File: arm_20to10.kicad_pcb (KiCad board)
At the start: 2 copper layers, 16.9 x 29.7 mm, 10 parts, among them J1 SFH11-PBPC-D10-RA-BK, J2 20021111-00010T4LF, SW1 SSSS810701, U1 MIC5504-3.3YM5 TR

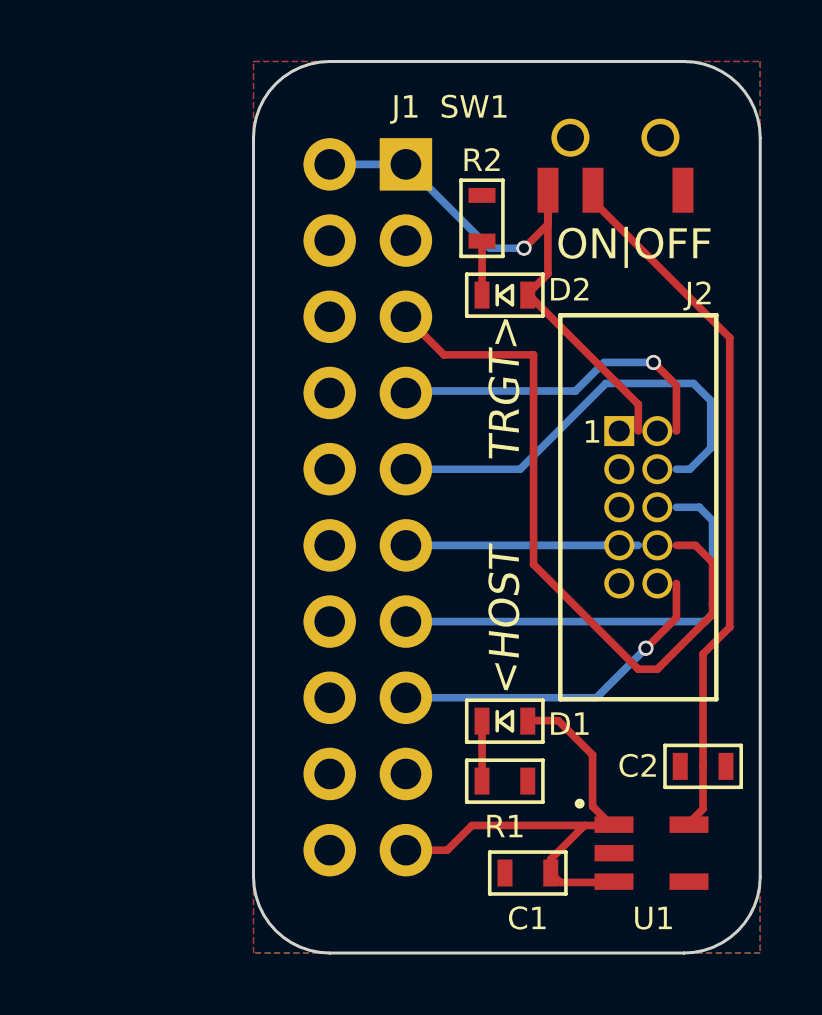
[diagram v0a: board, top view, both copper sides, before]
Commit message: Moved to the Kicad 9.0
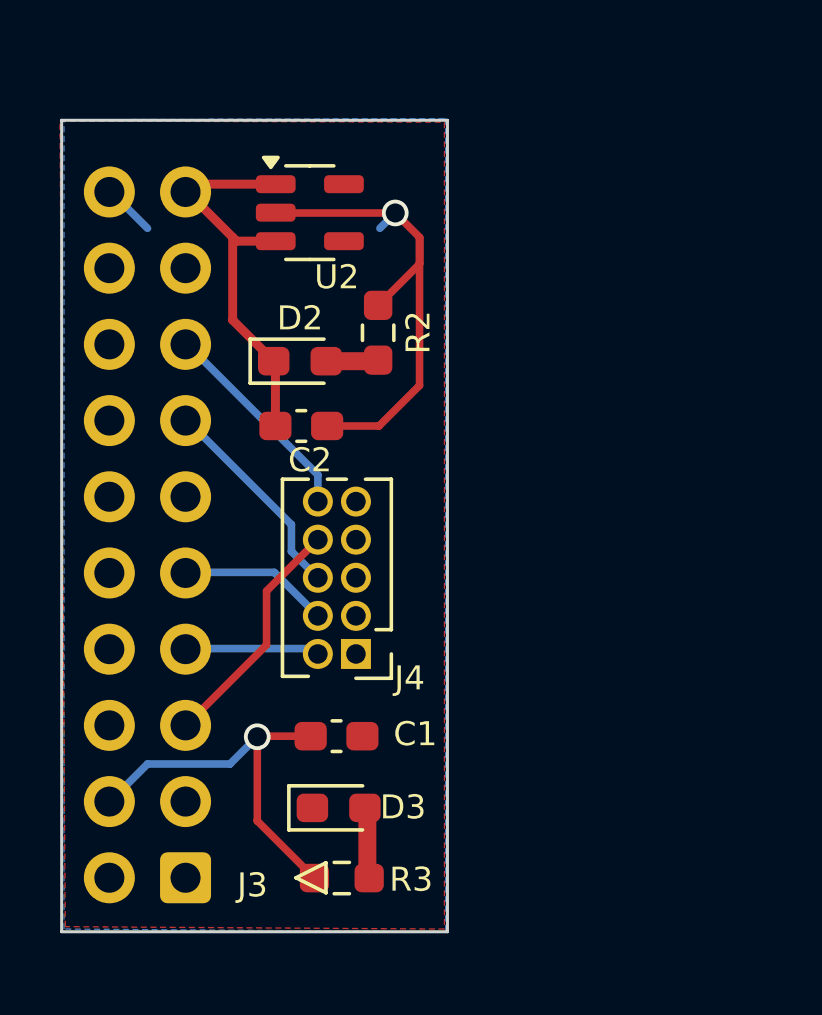
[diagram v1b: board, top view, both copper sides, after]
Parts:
- removed D1: LED, kicadlib:SMD_0603_LED
- removed J1: SFH11-PBPC-D10-RA-BK, kicadlib:ARM_20_PIN_TH_RIGHTANGLE
- removed J2: 20021111-00010T4LF, kicadlib:ARM_10_PIN
- removed R1: 1K, kicadlib:SMD_0603_R
- removed SW1: SSSS810701, kicadlib:SWITCH_SLIDE_SSSS810701
- removed U1: MIC5504-3.3YM5 TR, kicadlib:sot23-5_noah
- added D3: LED, LED_SMD:LED_0603_1608Metric_Pad1.05x0.95mm_HandSolder, F.Cu at (200.3, 176.4)
- added J3: Conn_ARM_JTAG_SWD_20, Connector_IDC:IDC-Header_2x10_P2.54mm_Vertical, F.Cu at (195.2, 178.7)
- added J4: Conn_ARM_JTAG_SWD_10, Connector_PinHeader_1.27mm:PinHeader_2x05_P1.27mm_Vertical, F.Cu at (200.9, 171.3)
- added R3: 1K, Resistor_SMD:R_0603_1608Metric_Pad0.98x0.95mm_HandSolder, F.Cu at (200.4, 178.7)
- added U2: MIC5504-3.3YM5, Package_TO_SOT_SMD:SOT-23-5, F.Cu at (199.4, 156.6)
- C1, C2: footprint kicadlib:SMD_0603_C -> Capacitor_SMD:C_0603_1608Metric_Pad1.08x0.95mm_HandSolder
- D2: footprint kicadlib:SMD_0603_LED -> LED_SMD:LED_0603_1608Metric_Pad1.05x0.95mm_HandSolder
- R2: value 500R -> 1K; footprint kicadlib:SMD_0603_R -> Resistor_SMD:R_0603_1608Metric_Pad0.98x0.95mm_HandSolder
- moved C2 17.0 mm to (199.1, 163.7), turned to 0 degrees
- moved C1 7.23 mm to (200.3, 174.0)
- moved D2 6.45 mm to (199.0, 161.5), turned to 0 degrees
- moved R2 4.61 mm to (201.6, 160.6)
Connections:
- C1 pad 1: /5V -> /VCC
- C2 pad 1: Net-(C2-Pad1) -> /5V
- C2 pad 2: Net-(C2-Pad2) -> GND
- D2 pad 1: /VCC -> /5V
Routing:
- net GND: track 0.00 -> 32.1 mm, vias 0 -> 2
- net Net-(SW1-Pad2): track 23.7 -> 0.00 mm
- net /VCC: track 19.8 -> 0.00 mm, vias 1 -> 0
- net /TDI: track 23.1 -> 7.98 mm
- net /SWO/TDO: track 14.9 -> 0.00 mm
- net /TCLK/SWCLK: track 14.6 -> 0.00 mm
- net /TMS/SWDIO: track 11.3 -> 0.00 mm, vias 1 -> 0
- net /NRST: track 11.3 -> 0.00 mm, vias 1 -> 0
- net /RTCK: track 8.13 -> 0.00 mm
- net /SRST: track 0.00 -> 7.07 mm
- net /SWO: track 0.00 -> 7.07 mm
- net /SWCLK: track 0.00 -> 4.97 mm
- net /SWDIO: track 0.00 -> 4.44 mm
- net Net-(D3-A): track 0.00 -> 2.40 mm
- net Net-(D1-Pad2): track 2.03 -> 0.00 mm
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- added copper zone on F.Cu, net /VCC
- removed copper zone on F.Cu, net GND
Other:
- board size 16.9 x 29.7 mm -> 12.9 x 27.1 mm
- net class Default removed
- board text removed: "<HOST"
- board text removed: "ON|OFF"
- board text removed: "TRGT>"
- board text removed: "github.com/noahp/arm_20to10 v2.1"
